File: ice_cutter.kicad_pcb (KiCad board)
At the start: 4 copper layers, 90 x 100 mm, 188 parts, among them J1 Conn_01x01_Male, J2 Barrel_Jack, J3 pot, J4 Conn_01x01_Male, J5 program, J6 program2, J7 hands, J8 UART, J9 xt60, M1 Motor_Servo, M2 Motor_Servo, Q1 Q_PMOS_GSD, Q10 S8050_SMD, Q11 Q_NMOS_GSD, Q12 Q_NMOS_GSD, Q13 Q_NMOS_GSD, Q14 Q_NMOS_GSD, Q15 S8550, Q16 S8050_SMD, Q17 S8050_SMD, Q18 S8050_SMD, Q2 Q_PMOS_GSD, Q3 Q_PMOS_GSD, Q4 S8550, Q5 Q_NMOS_GSD, Q6 S8550, Q7 Q_NMOS_GSD, Q8 S8050_SMD, Q9 S8050_SMD, SW1 SW_Push, SW2 SW_Push, SW3 SW_Push, U1 LM317_TO-252, U10 TMP117, U11 TM1620, U12 INA219AxD, U2 LM317_TO-252, U3 INA219AxD, U4 LM317_TO-252, U5 INA219AxD, U6 FJ4301AH, U7 FJ4301AH, U8 STM32G030XX, U9 SHT30-DIS

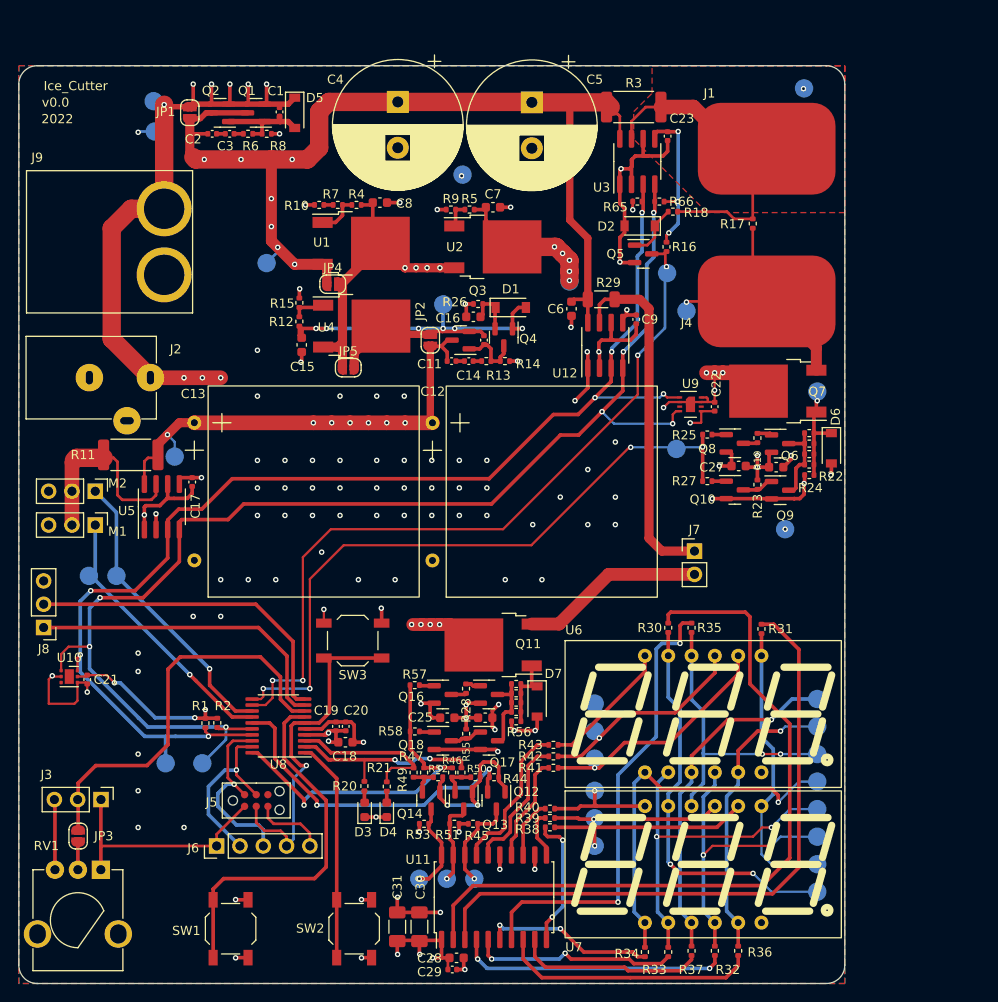
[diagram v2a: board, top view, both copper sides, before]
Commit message: major schematic changes, 5V is now the highest voltage, added more FETs for Wire conduction, more for SS, opamp for current hack, removed Regs, XT60 and significantly changed wiring and R values for sections... Still a lot to be done, cant be solved now
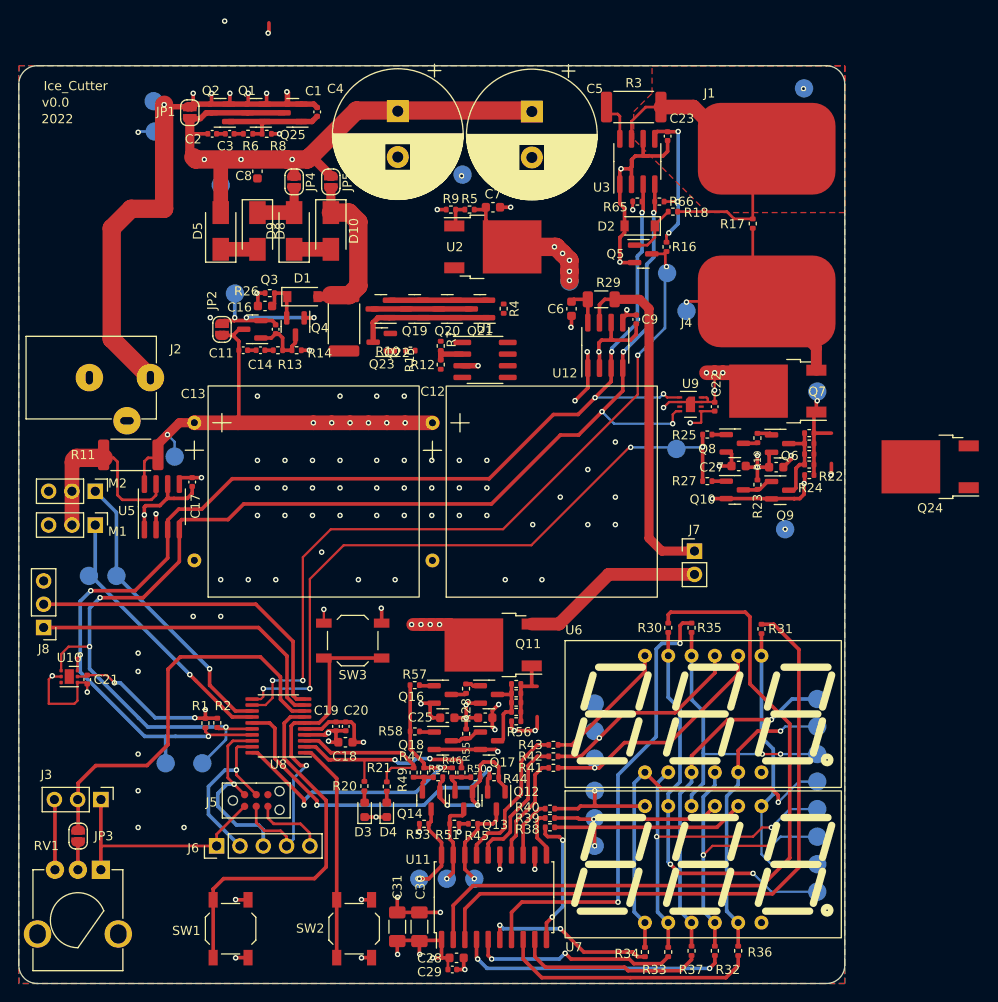
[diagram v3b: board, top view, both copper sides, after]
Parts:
- removed C15: 10u, Capacitor_SMD:C_0603_1608Metric
- removed D6, D7: 10V, Diode_SMD:D_SOD-123
- removed J9: xt60, UCT:XT60PW-M
- removed U4: LM317_TO-252, Package_TO_SOT_SMD:TO-252-2
- added D10: 5554, Diode_SMD:D_SMA, F.Cu at (102.4, 47.4)
- added D8: 5554, Diode_SMD:D_SMA, F.Cu at (94.4, 47.4)
- added D9: 5554, Diode_SMD:D_SMA, F.Cu at (98.4, 47.4)
- added Q19: Q_PMOS_GSD, Package_TO_SOT_SMD:SOT-23, F.Cu at (111.5, 55.9)
- added Q20: Q_PMOS_GSD, Package_TO_SOT_SMD:SOT-23, F.Cu at (115.1, 55.9)
- added Q21: Q_PMOS_GSD, Package_TO_SOT_SMD:SOT-23, F.Cu at (118.6, 55.9)
- added Q22: Q_PMOS_GSD, Package_TO_SOT_SMD:SOT-23, F.Cu at (107.8, 55.9)
- added Q23: S8050_SMD, Package_TO_SOT_SMD:SOT-23, F.Cu at (107.9, 59.5)
- added Q24: Q_NMOS_GSD, Package_TO_SOT_SMD:TO-252-2, F.Cu at (167.7, 73.1)
- added Q25: Q_PMOS_GSD, Package_TO_SOT_SMD:SOT-23, F.Cu at (98.2, 34.5)
- D5: value 10V -> 5554; footprint Diode_SMD:D_SOD-123 -> Diode_SMD:D_SMA
- R10: value 1k5 -> 4k7
- R12, R4: value 220R -> 3.3M
- R15: value 680R -> 1R; footprint Resistor_SMD:R_0402_1005Metric -> Resistor_SMD:R_2512_6332Metric
- R19, R23, R28, R55: value 4k7 -> 1k5
- R7: value 220R -> 1k
- U1: value LM317_TO-252 -> LM358; footprint Package_TO_SOT_SMD:TO-252-2 -> Package_SO:SOIC-8_3.9x4.9mm_P1.27mm
- moved C14 22.7 mm to (94.7, 60.4)
- moved D1 22.7 mm to (99.3, 54.6)
- moved Q4 22.7 mm to (98.5, 57.8)
- moved R13 22.7 mm to (96.6, 60.4)
- moved R26 22.7 mm to (95.7, 54.2)
- moved C10 22.7 mm to (96.3, 58.1)
- moved JP2 22.7 mm to (90.5, 58.1)
- moved TP21 22.7 mm to (91.9, 54.2)
- moved C11 22.7 mm to (92.8, 60.4)
- moved R14 22.7 mm to (98.6, 60.4)
- moved C16 22.7 mm to (95.2, 55.6)
- moved Q3 22.7 mm to (93.8, 58.1)
- moved JP5 20.3 mm to (102.4, 42.1), turned to -90 degrees
- moved R4 19.6 mm to (121.2, 55.9), turned to -90 degrees
- moved R7 19.0 mm to (114.3, 59.9), turned to -90 degrees
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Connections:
- C10 pad 1: +5V -> Net-(C10-Pad1)
- C11 pad 1: /5V_SS -> /LV
- C12 pad 1: /5V_SS -> /LV
- C13 pad 1: /5V_SS -> /LV
- C24 pad 1: +12V -> /V_SS
- C25 pad 1: +12V -> /V_SS
- C26 pad 1: +12V -> /V_SS
- C27 pad 1: +12V -> /V_SS
- C8 pad 1: +12V -> /V_SS
- D1 pad 2: +5V -> /LV_Out
- D5 pad 1: VDC -> Net-(D5-Pad1)
- D5 pad 2: /SS_FET -> /V_SS
- JP2 pad 1: +5V -> Net-(C10-Pad1)
- JP2 pad 2: /5V_SS -> /LV
- JP4 pad 2: +12V -> Net-(D8-Pad1)
- JP5 pad 1: +12V -> /V_SS
- JP5 pad 2: +5V -> /LV_Out
- Q15 pad 2: +12V -> /V_SS
- Q3 pad 2: +5V -> Net-(C10-Pad1)
- Q3 pad 3: /5V_SS -> /LV
- Q4 pad 1: +5V -> Net-(C10-Pad1)
- Q6 pad 2: +12V -> /V_SS
- R10 pad 1: GND -> Net-(Q23-Pad1)
- R11 pad 1: /5V_SS -> /V_SS
- R12 pad 2: +5V -> GND
- R15 pad 1: GND -> /LV_Out
- R15 pad 2: Net-(R12-Pad1) -> Net-(C10-Pad1)
- R23 pad 2: +12V -> /V_SS
- R3 pad 1: /V_SS -> /LV
- R4 pad 1: Net-(R4-Pad1) -> /LV_Out
- R4 pad 2: +12V -> /Gate
- R55 pad 2: +12V -> /V_SS
- R7 pad 1: Net-(R10-Pad2) -> /V_SS
- R7 pad 2: Net-(R4-Pad1) -> Net-(R12-Pad1)
- U1 pad 1: Net-(R4-Pad1) -> Net-(R10-Pad2)
- U1 pad 2: +12V -> Net-(R12-Pad1)
- U1 pad 3: /V_SS -> /5V_SS
- U2 pad 3: +12V -> /V_SS
- U3 pad 8: /V_SS -> /LV
- U5 pad 8: /5V_SS -> /V_SS
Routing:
- net +12V: track 151.9 -> 0.00 mm, vias 8 -> 0
- net /V_SS: track 114.2 -> 190.8 mm
- net /LV: track 0.00 -> 66.7 mm, vias 0 -> 7
- net +5V: track 53.4 -> 0.00 mm, vias 6 -> 0
- net /5V_SS: track 68.0 -> 22.1 mm, vias 12 -> 6
- net /LV_Out: track 0.00 -> 28.8 mm
- net +3V3: track 158.4 -> 130.3 mm
- net Net-(C10-Pad1): track 0.00 -> 17.7 mm, vias 0 -> 4
- net /Gate: track 0.00 -> 14.9 mm
- net VDC: track 71.3 -> 62.3 mm, vias 9 -> 7
- net Net-(D8-Pad1): track 0.00 -> 6.70 mm
- net Net-(R4-Pad1): track 4.65 -> 0.00 mm
- net Net-(D5-Pad1): track 0.00 -> 4.00 mm
- net Net-(D10-Pad2): track 0.00 -> 4.00 mm
- net GND: track 180.8 -> 177.4 mm, vias 107 -> 104
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
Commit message: more mods, taking it to a solution. Mostly on layer 3 and power management
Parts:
- added C15: 100n, Capacitor_SMD:C_0402_1005Metric, F.Cu at (123.9, 61.3)
- R12: value 3.3M -> 4k7
- R7: value 1k -> 220R
- moved TP22 23.3 mm to (106.8, 63.0)
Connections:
- C28 pad 1: /5V_SS -> /V_SS
- C29 pad 1: /5V_SS -> /V_SS
- C30 pad 1: /5V_SS -> /V_SS
- C31 pad 1: /5V_SS -> /V_SS
- R12 pad 1: Net-(R12-Pad1) -> GND
- R12 pad 2: GND -> Net-(U1-Pad2)
- R45 pad 2: /5V_SS -> /V_SS
- R51 pad 2: /5V_SS -> /V_SS
- R53 pad 2: /5V_SS -> /V_SS
- R7 pad 1: /V_SS -> Net-(U1-Pad2)
- R7 pad 2: Net-(R12-Pad1) -> /LV_Out
- U1 pad 2: Net-(R12-Pad1) -> Net-(U1-Pad2)
- U11 pad 1: /5V_SS -> /V_SS
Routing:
- net /V_SS: track 190.8 -> 140.0 mm, vias 7 -> 23
- net +3V3: track 130.3 -> 158.2 mm, vias 22 -> 19
- net /5V_SS: track 22.1 -> 6.29 mm, vias 6 -> 1
- net /LV: track 66.7 -> 53.5 mm, vias 7 -> 6
- net GND: track 177.4 -> 188.0 mm
- net Net-(U1-Pad2): track 0.00 -> 3.36 mm
- net Net-(R12-Pad1): track 3.36 -> 0.00 mm
- net VDC: track 62.3 -> 63.5 mm
- added copper zone on In2.Cu, net /LV
- removed copper zone on In2.Cu, net /5V_SS
